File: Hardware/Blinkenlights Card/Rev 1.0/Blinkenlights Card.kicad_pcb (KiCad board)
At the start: 2 copper layers, 100 x 57.6 mm, 76 parts, among them J1 6502 Card Edge, U1 74HC573, U2 74HC573, U3 74HC04, U4 74HC573

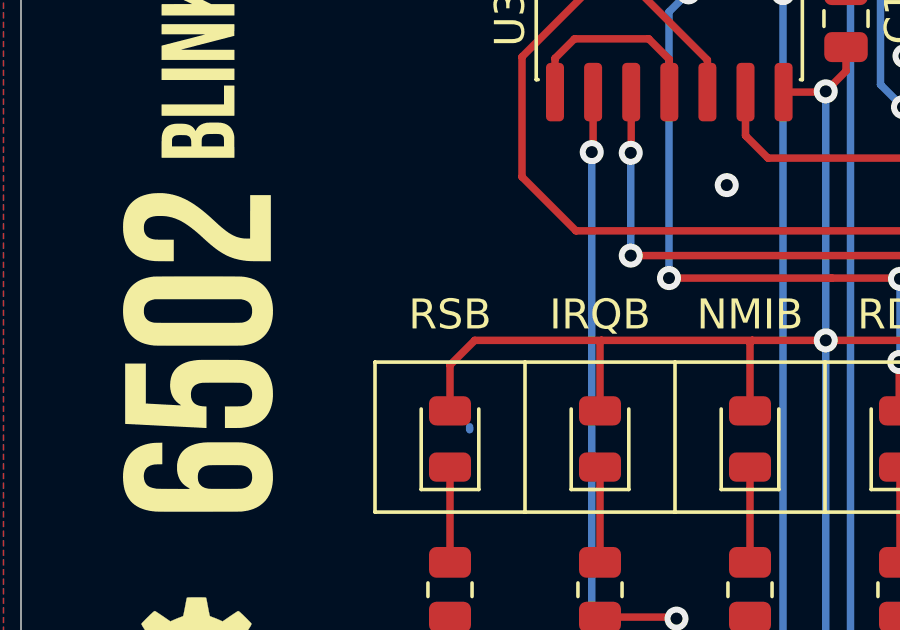
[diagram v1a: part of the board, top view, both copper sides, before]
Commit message: Silkscreen fix
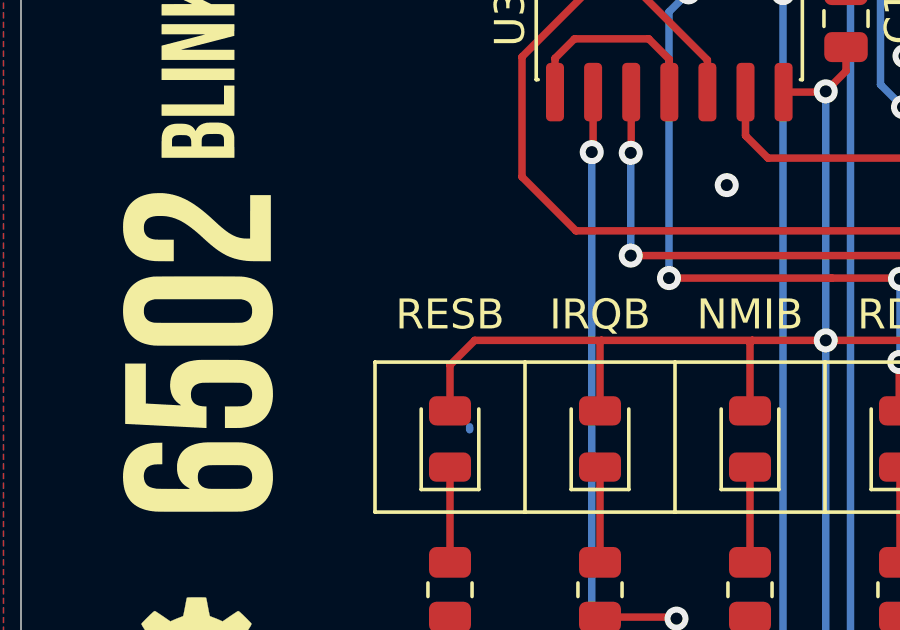
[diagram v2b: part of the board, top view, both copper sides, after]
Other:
- board text added: "RESB"
- board text removed: "RSB"
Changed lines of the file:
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@@
 		)
 	)
-	(gr_text "RSB"
+	(gr_text "RESB"
 		(at 112.8011 109.8136 0)
 		(layer "F.SilkS")
